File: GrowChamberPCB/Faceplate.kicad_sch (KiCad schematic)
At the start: 52 parts, among them J1 Mister, J10 FoggerBasin, J12 Moisture Sensor 3, J13 Moisture Sensor 2, J14 UART, J15 FAE Fan, J16 DrainLevel, J2 Moisture Sensor 1, J3 SCD30, J4 Heater Fans, J5 Fogger Solenoid, J6 Drain Solenoid, J7 Water Solenoid, J8 Glycol Solenoid, J9 CircFan, SW2 ResetButton_External, SW4 BootMode_External, U19 To Faceplate, U20 PCA9555APW,118

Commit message: Removed 3.3V, wired some stuff
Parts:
- removed R35, R43: 270, easyeda2kicad:R0603, symbol easyeda2kicad:0603WAF2700T5E
- added R35, R43: 1k, easyeda2kicad:R0603, symbol easyeda2kicad:FRC0603J102TS
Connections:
- net 12V_FP: now also R35.2, R43.2
- net at LED11.2 (A): now also R43.1
- net at LED10.2 (A): now also R35.1
- net 5V_FP: no longer names the net of U20.24 (VDD)
- net 5V_FP: no longer U19.14

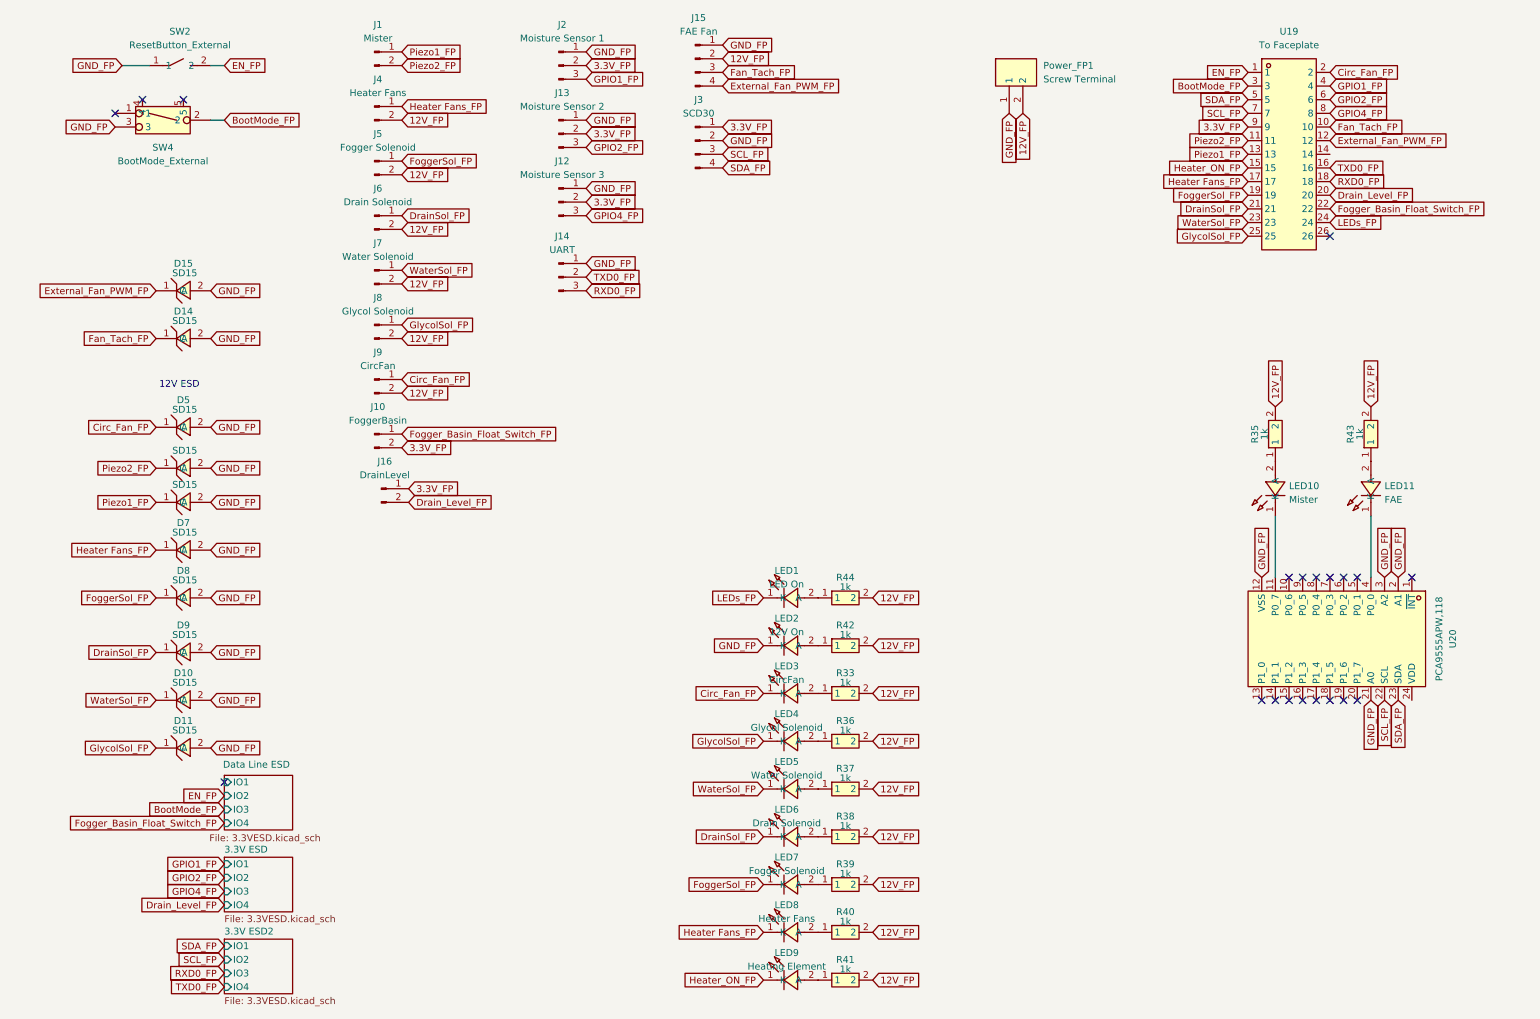
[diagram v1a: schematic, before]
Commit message: failing to route the board
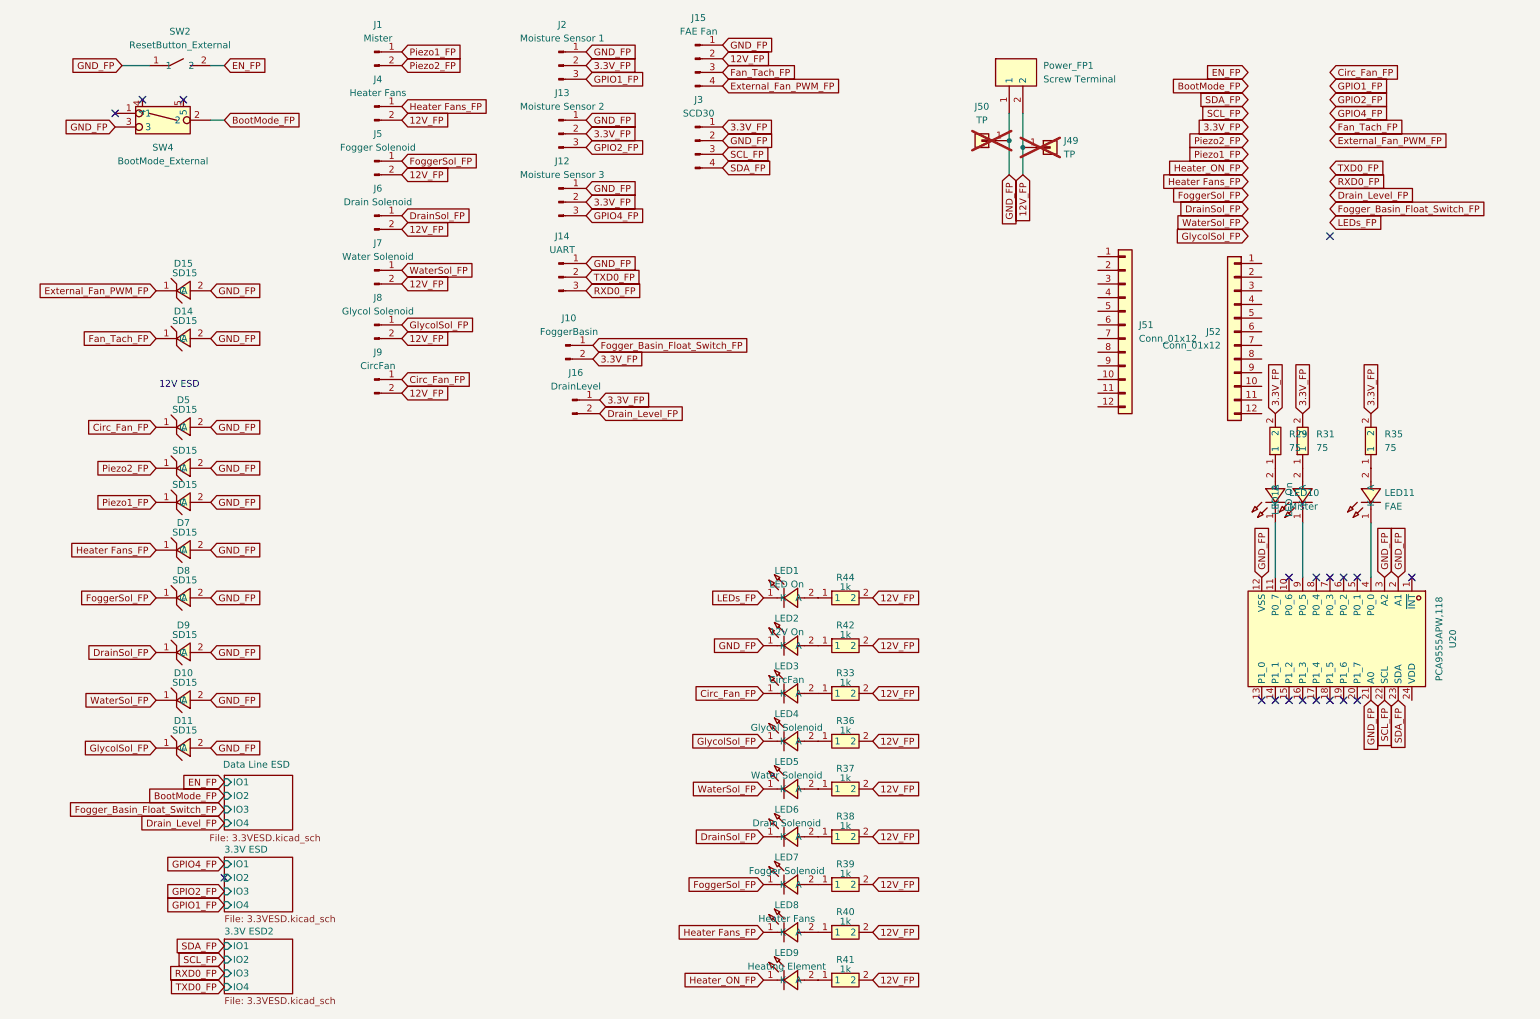
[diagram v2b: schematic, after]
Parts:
- removed R35, R43: 1k, easyeda2kicad:R0603, symbol easyeda2kicad:FRC0603J102TS
- removed U19: To Faceplate, easyeda2kicad:IDC-TH_26P-P2.54_ZX-IDC2.54-2-13PZZ, symbol easyeda2kicad:ZX-IDC2.54-2-13PZZ
- added J49: TP, TestPoint:TestPoint_Pad_D2.0mm, symbol Connector_Generic:Conn_01x01
- added J50: TP, TestPoint:TestPoint_THTPad_2.0x2.0mm_Drill1.0mm, symbol Connector_Generic:Conn_01x01
- added J51, J52: Conn_01x12, Connector_PinSocket_2.54mm:PinSocket_1x12_P2.54mm_Vertical, symbol Connector_Generic:Conn_01x12
- added LED12: LED On, easyeda2kicad:LED-TH_BD3.9-P2.54-RD_RED, symbol easyeda2kicad:EL304RD
- added R29, R31, R35: 75, easyeda2kicad:R0603, symbol easyeda2kicad:RS-03K75R0FT
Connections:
- net 12V_FP: now also J49.1 (Pin_1)
- net 3.3V_FP: now also R29.2, R31.2, R35.2
- net GND_FP: now also J50.1 (Pin_1)
- net at U20.9 (P0_5): now also LED12.1 (K)
- net at LED11.2 (A): now also R35.1
- net at LED10.2 (A): now also R29.1
- new net: LED12.2 (A), R31.1
- no-connect marks 20 -> 19
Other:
- moved on the sheet: J10, J16, LED10, LED11

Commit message: almost done routing
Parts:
- removed J51, J52: Conn_01x12, Connector_PinSocket_2.54mm:PinSocket_1x12_P2.54mm_Vertical, symbol Connector_Generic:Conn_01x12
- added U2: ZX-IDC2.54-2-13PZZ, easyeda2kicad:IDC-TH_26P-P2.54_ZX-IDC2.54-2-13PZZ, symbol easyeda2kicad:ZX-IDC2.54-2-13PZZ

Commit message: working on pcb
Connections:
- net 3.3V_FP: now also U20.24 (VDD)
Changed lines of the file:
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@@
+		)
+	)
+	(global_label "3.3V_FP"
+		(shape input)
+		(at 265.43 139.7 270)
+		(fields_autoplaced yes)
+		(effects
+			(font
+				(size 1.27 1.27)
+			)
+			(justify right)
+		)
+		(property "Intersheetrefs" "${INTERSHEET_REFS}"
+			(at 265.43 150.1238 90)
+			(hide yes)
+			(show_name no)
+			(do_not_autoplace no)
+			(effects
+				(font
+					(size 1.27 1.27)
+				)
+				(justify right)
+			)
 		)
 	)

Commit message: fillin stuff out
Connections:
- net 3.3V_FP: now also U2.2, U2.4
- net BootMode_FP: now also U2.8
- net Circ_Fan_FP: now also U2.19
- net DrainSol_FP: now also U2.17
- net Drain_Level_FP: now also U2.16
- net EN_FP: now also U2.6
- net External_Fan_PWM_FP: now also U2.24
- net Fan_Tach_FP: now also U2.26
- net FoggerSol_FP: now also U2.13
- net Fogger_Basin_Float_Switch_FP: now also U2.18
- net GPIO1_FP: no longer J2.3 (Pin_3)
- net GPIO2_FP: no longer J13.3 (Pin_3)
- net GPIO4_FP: no longer J12.3 (Pin_3)
- net GlycolSol_FP: now also U2.11
- net Heater Fans_FP: now also U2.15
- net Heater_ON_FP: now also U2.5
- net LEDs_FP: now also U2.7
- net Piezo1_FP: now also U2.3
- net Piezo2_FP: now also U2.1
- net RXD0_FP: now also U2.20
- net SCL_FP: now also U2.25
- net SDA_FP: now also U2.23
- net TXD0_FP: now also U2.22
- net WaterSol_FP: now also U2.9
- net SoilMoisture4_FP: now reaches U2.10
- net SoilMoisture4_FP: now also J12.3 (Pin_3)
- net SoilMoisture2_FP: now reaches U2.12
- net SoilMoisture2_FP: now also J13.3 (Pin_3)
- net SoilMoisture1_FP: now reaches U2.14
- net SoilMoisture1_FP: now also J2.3 (Pin_3)

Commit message: redesign 3
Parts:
- J1, J10, J12, J13, J14, J15, J16, J2, J3, J4, J5, J6, J7, J8, J9: now not fitted; now left out of the parts list
